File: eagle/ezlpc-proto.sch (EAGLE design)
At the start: 62 parts, among them J1 MICRO USB, Q1 12Mhz, T1 MMBT3906, U1 PRTR5V0U2X, U2 MIC5225-3.3v, U3 LPC11U35FHN33/501

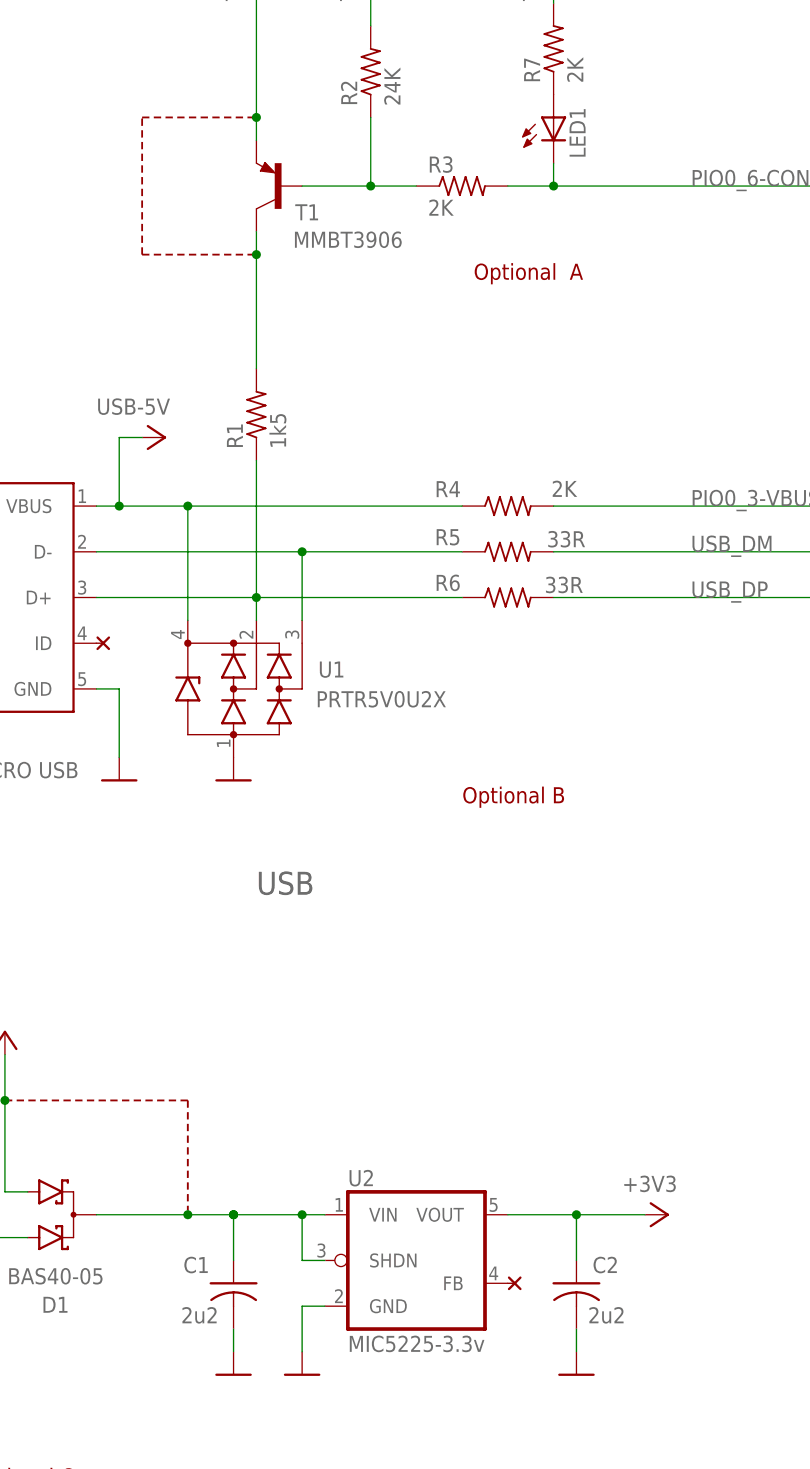
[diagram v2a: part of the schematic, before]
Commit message: Extracted self library from the schema.
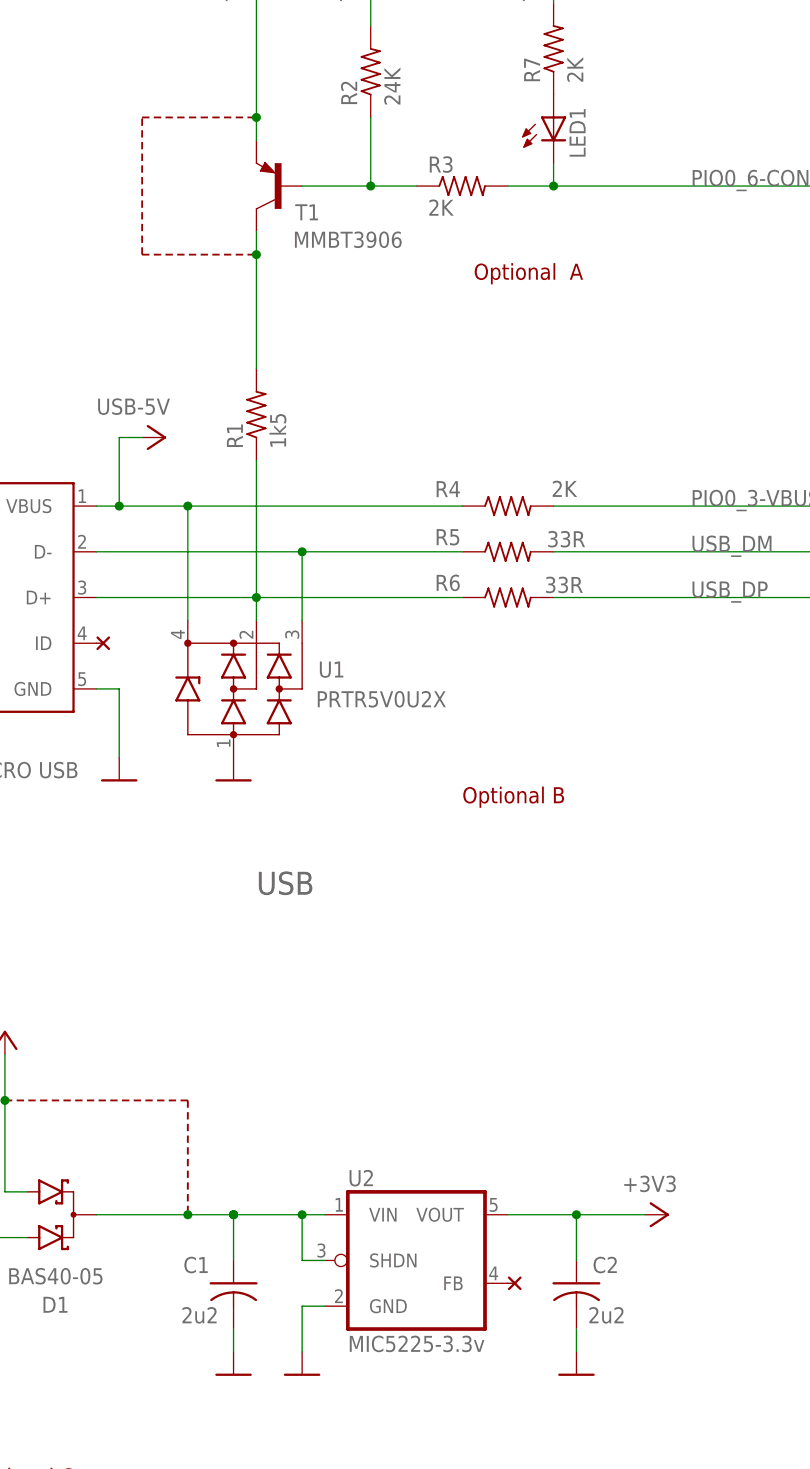
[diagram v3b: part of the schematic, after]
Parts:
- C1, C2: device rcl:C-USC0603K -> ezlpc-proto:CAPACITORC0603K
- T1: device transistor-pnp:MMBT3906LT1SMD -> ezlpc-proto:BC857B-PNP-SOT23-BEC
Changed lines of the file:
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@@
 <part name="U2" library="ezlpc-proto" deviceset="TC1015" device="" value="MIC5225-3.3v"/>
 <part name="GND3" library="ezlpc-proto" deviceset="GND" device=""/>
-<part name="C2" library="rcl" deviceset="C-US" device="C0603K" value="2u2"/>
+<part name="C2" library="ezlpc-proto" deviceset="CAPACITOR" device="C0603K" value="2u2"/>
 <part name="GND18" library="ezlpc-proto" deviceset="GND" device=""/>
-<part name="C1" library="rcl" deviceset="C-US" device="C0603K" value="2u2"/>
+<part name="C1" library="ezlpc-proto" deviceset="CAPACITOR" device="C0603K" value="2u2"/>
 <part name="GND28" library="ezlpc-proto" deviceset="GND" device=""/>
 <part name="U3" library="ezlpc-proto" deviceset="LPC11U35FHN33/501" device=""/>
@@
 <part name="U$1" library="ezlpc-proto" deviceset="NC" device=""/>
 <part name="U$2" library="ezlpc-proto" deviceset="NC" device=""/>
-<part name="T1" library="transistor-pnp" deviceset="MMBT3906*" device="SMD" technology="LT1" value="MMBT3906"/>
+<part name="T1" library="ezlpc-proto" deviceset="*-PNP-" device="SOT23-BEC" technology="BC857B" value="MMBT3906"/>
 <part name="JP31" library="ezlpc-proto" deviceset="PINHD-1X1" device=""/>
 <part name="JP32" library="ezlpc-proto" deviceset="PINHD-1X1" device=""/>

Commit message: Ready for final auto routing.
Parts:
- removed JP32: (no value), ezlpc-proto:PINHD-1X1
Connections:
- net GND: no longer JP32.1
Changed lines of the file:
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@@
 <part name="T1" library="ezlpc-proto" deviceset="*-PNP-" device="SOT23-BEC" technology="BC857B" value="MMBT3906"/>
 <part name="JP31" library="ezlpc-proto" deviceset="PINHD-1X1" device=""/>
-<part name="JP32" library="ezlpc-proto" deviceset="PINHD-1X1" device=""/>
-<part name="GND7" library="ezlpc-proto" deviceset="GND" device=""/>
 </parts>
 <sheets>
@@
 </instance>
 <instance part="JP31" gate="G$1" x="294.64" y="127"/>
-<instance part="JP32" gate="G$1" x="294.64" y="124.46"/>
-<instance part="GND7" gate="1" x="289.56" y="121.92"/>
 </instances>
 <busses>
@@
 <wire x1="190.5" y1="154.94" x2="190.5" y2="152.4" width="0.1524" layer="91"/>
 </segment>
-<segment>
-<pinref part="JP32" gate="G$1" pin="1"/>
-<pinref part="GND7" gate="1" pin="GND"/>
-<wire x1="292.1" y1="124.46" x2="289.56" y2="124.46" width="0.1524" layer="91"/>
-</segment>
 </net>

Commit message: Cleaned up tplace text.
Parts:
- U3: value LPC11U35FHN33/501 -> LPC11U35FHI33/501
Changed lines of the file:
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@@
 <part name="C1" library="ezlpc-proto" deviceset="CAPACITOR" device="C0603K" value="2u2"/>
 <part name="GND28" library="ezlpc-proto" deviceset="GND" device=""/>
-<part name="U3" library="ezlpc-proto" deviceset="LPC11U35FHN33/501" device=""/>
+<part name="U3" library="ezlpc-proto" deviceset="LPC11U35FHN33/501" device="" value="LPC11U35FHI33/501"/>
 <part name="GND2" library="ezlpc-proto" deviceset="GND" device=""/>
 <part name="Q1" library="ezlpc-proto" deviceset="CRYSTAL" device="CTS406" value="12Mhz"/>

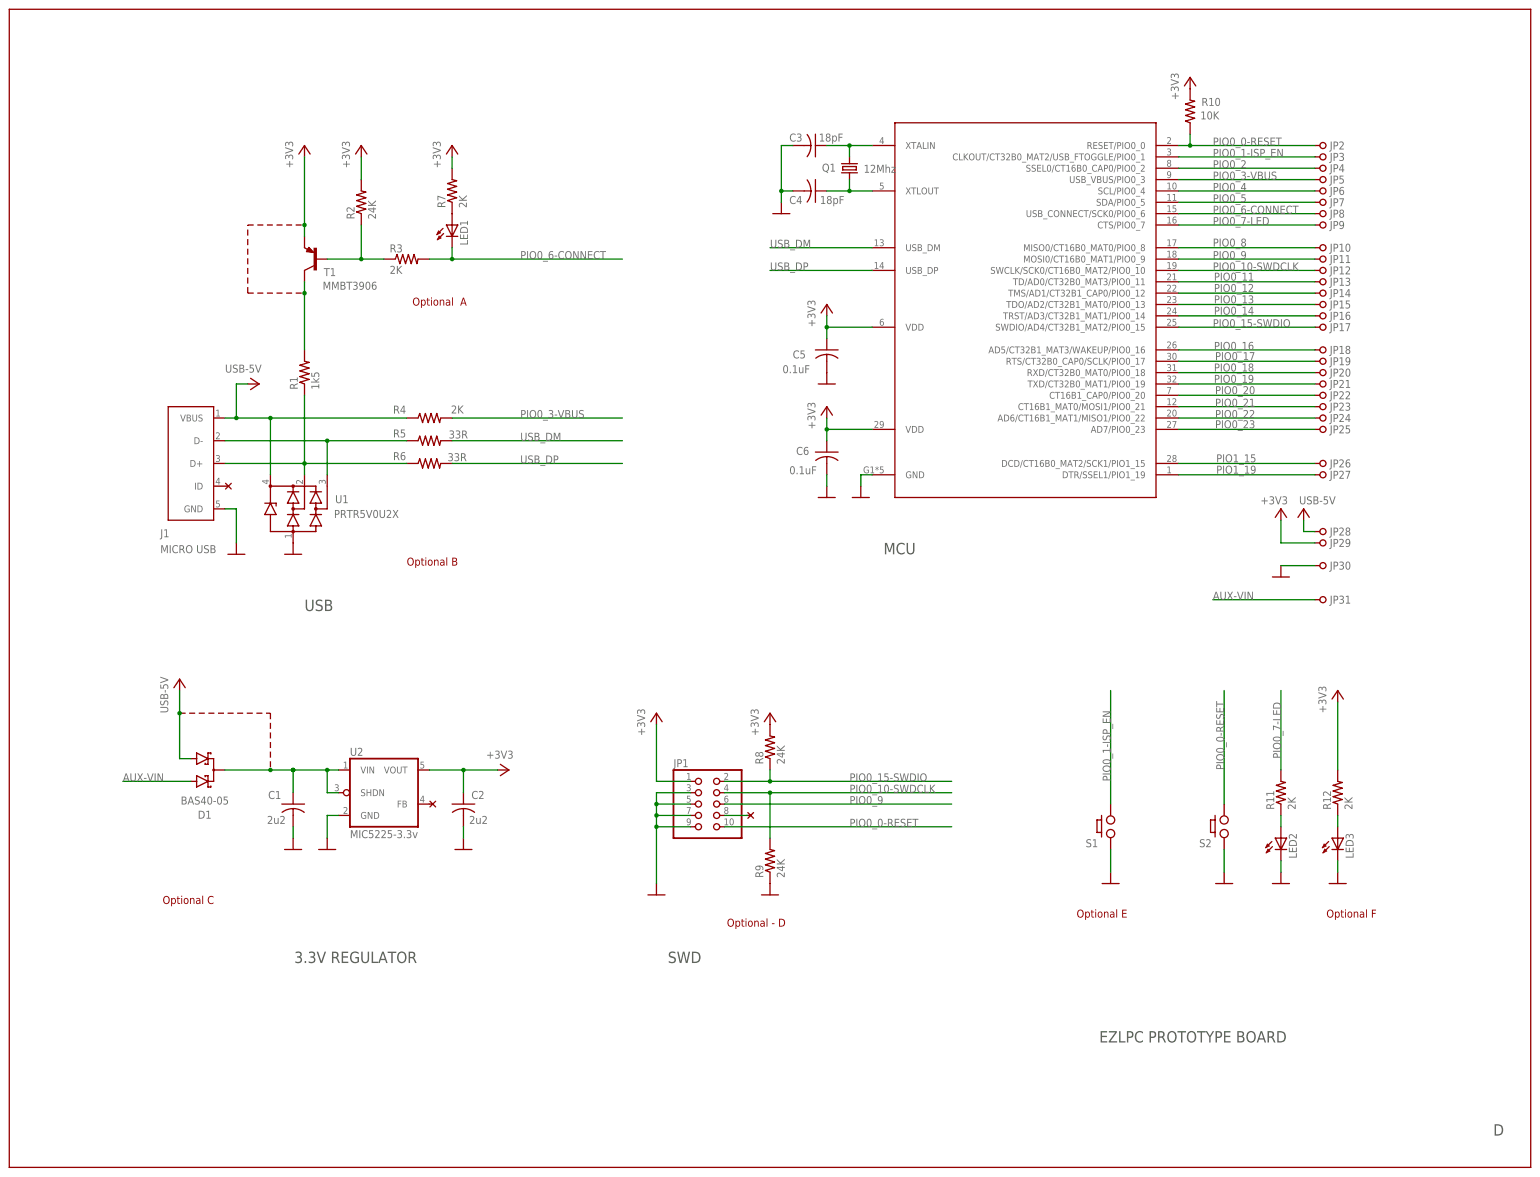
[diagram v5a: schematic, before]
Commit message: More layout cleanup.
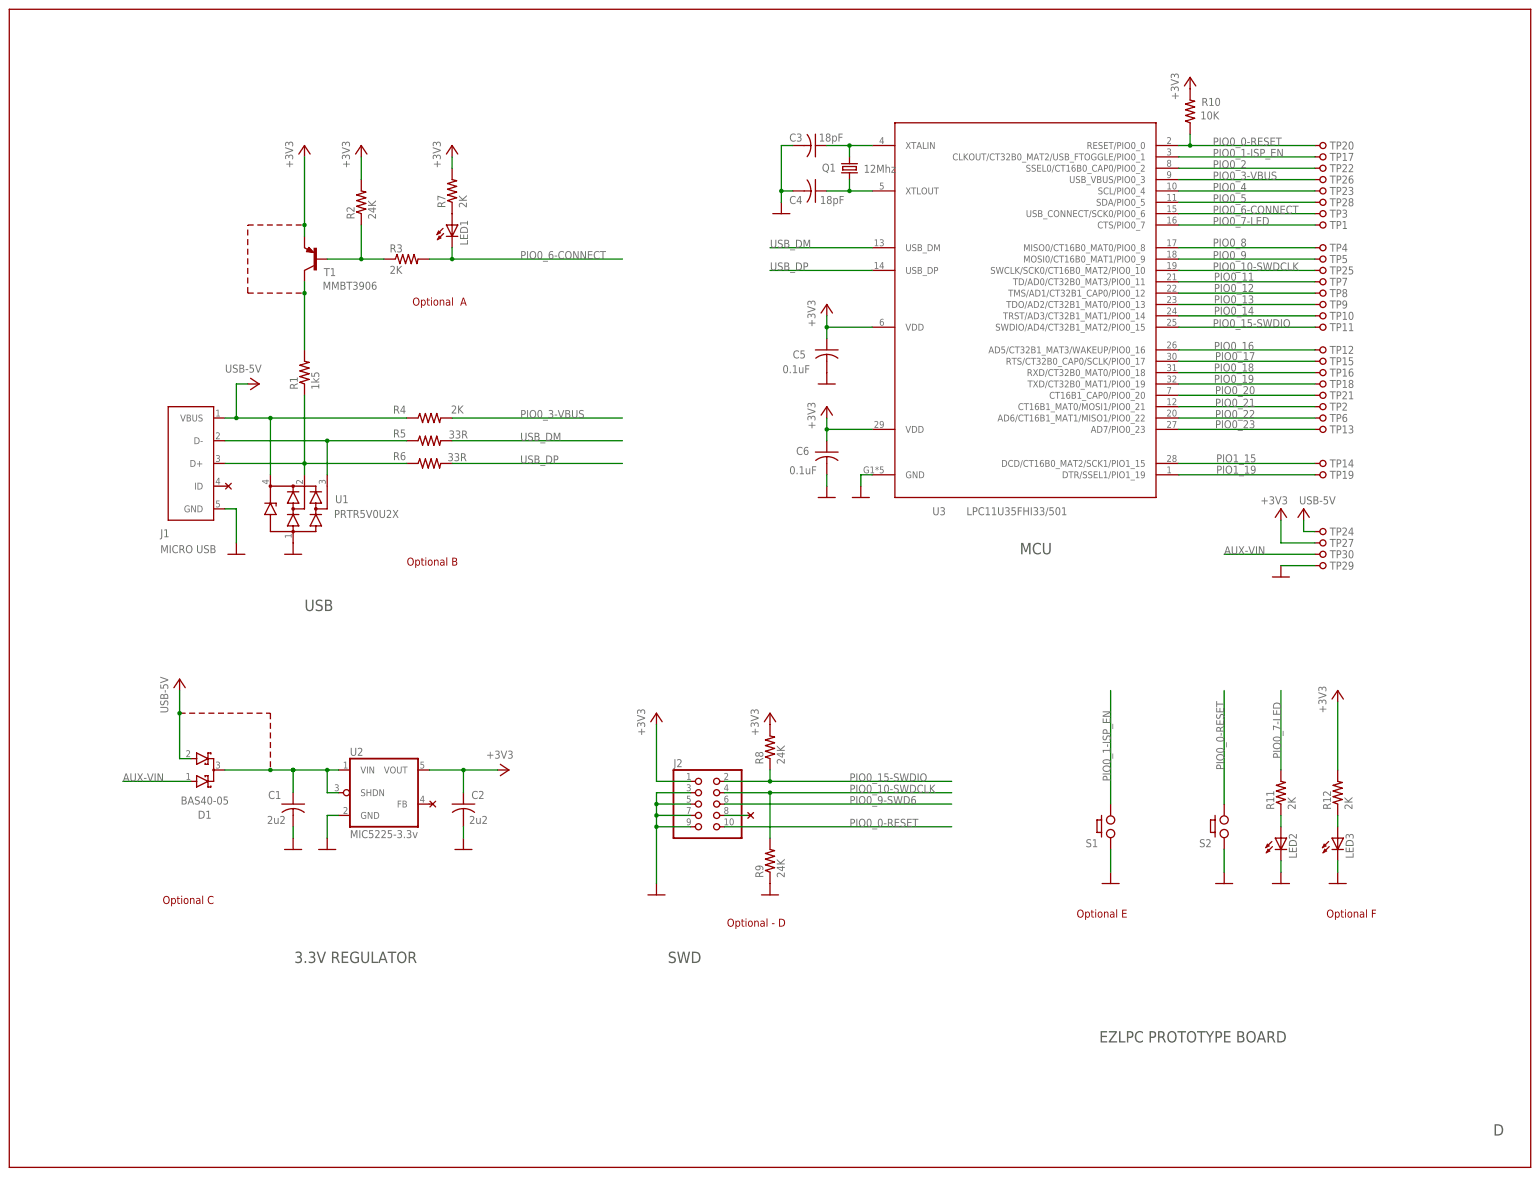
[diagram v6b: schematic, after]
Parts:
- removed JP31: (no value), ezlpc-proto:PINHD-1X1
- added TP30: (no value), ezlpc-proto:PINHD-1X1
- renumbered JP1 to J2, JP10 to TP4, JP11 to TP5, JP12 to TP25, JP13 to TP7, JP14 to TP8, JP15 to TP9, JP16 to TP10, JP17 to TP11, JP18 to TP12, JP19 to TP15, JP2 to TP20, JP20 to TP16, JP21 to TP18, JP22 to TP21, JP23 to TP2, JP24 to TP6, JP25 to TP13, JP26 to TP14, JP27 to TP19, JP28 to TP24, JP29 to TP27, JP3 to TP17, JP30 to TP29, JP4 to TP22, JP5 to TP26, JP6 to TP23, JP7 to TP28, JP8 to TP3, JP9 to TP1
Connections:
- new net PIO0_9-SWD6: J2.6
- net AUX-VIN: now also TP30.1; no longer JP31.1
- net PIO0_9: no longer J2.6
